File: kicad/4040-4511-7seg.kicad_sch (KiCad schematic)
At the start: 10 parts, among them U10 4040, U11 4511, U12 TDSR-3163-G

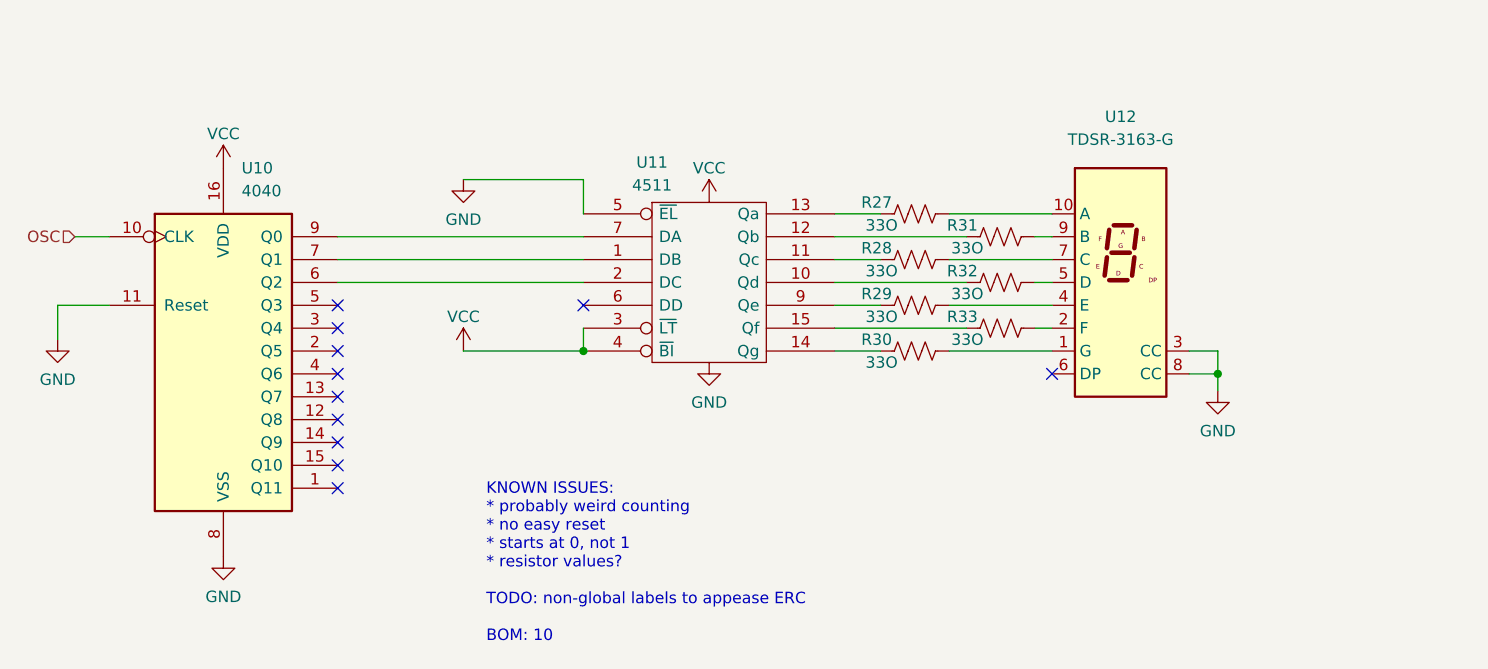
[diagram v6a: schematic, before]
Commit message: Fix missing 4511 BCD pin
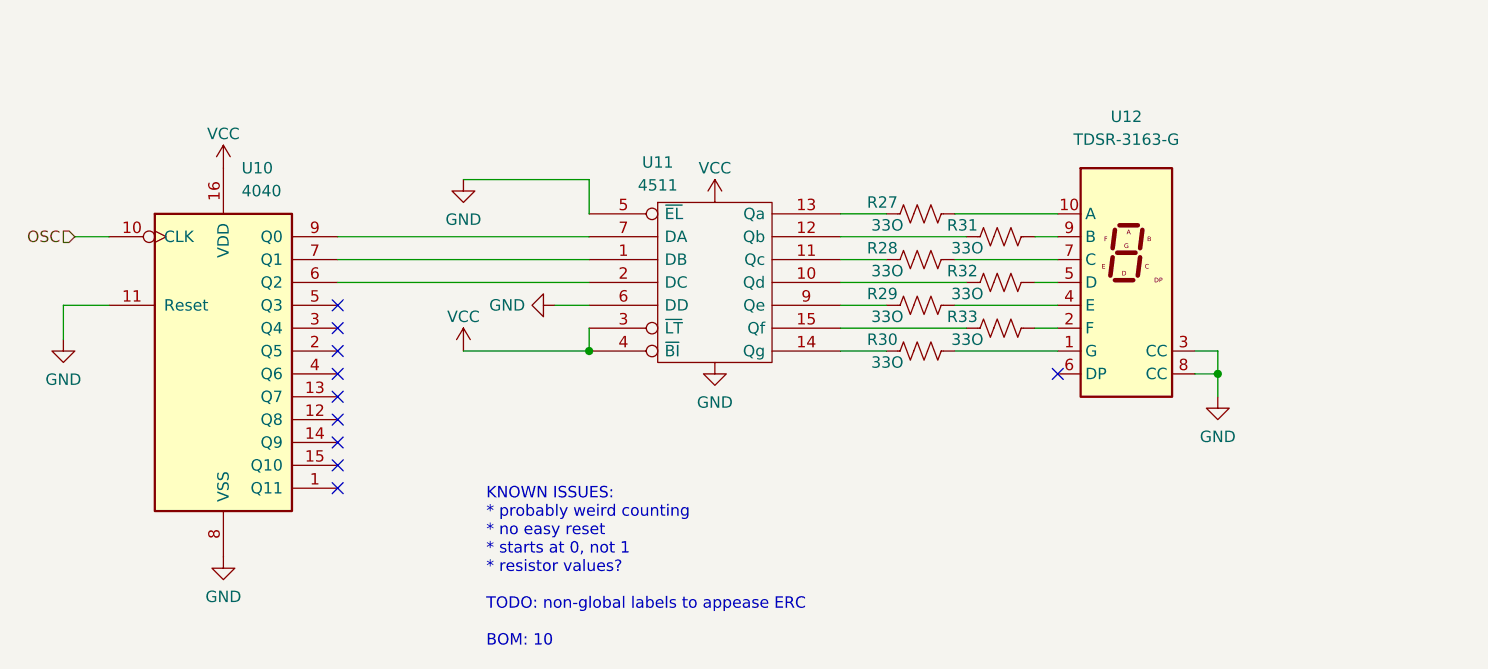
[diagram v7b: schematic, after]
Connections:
- net GND: now also U11.6 (DD)
- no-connect marks 11 -> 10
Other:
- moved on the sheet: R27, R28, R29, R30, U11, U12
